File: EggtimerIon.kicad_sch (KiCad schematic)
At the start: 46 parts, among them J1 Conn_01x02, J2 Conn_01x03, J3 B2B-PH-K-S, J4 USB_C_Receptacle_USB2.0, Q1 IRLML6244, Q2 2N7002, Q3 2N7002, U1 ESP32-WROOM-32-N4, U2 MPU-6050, U3 MS5611-01BA, U4 CAT24C512XI-T2, U5 AP2112K-3.3, U6 CP2102N-Axx-xQFN28

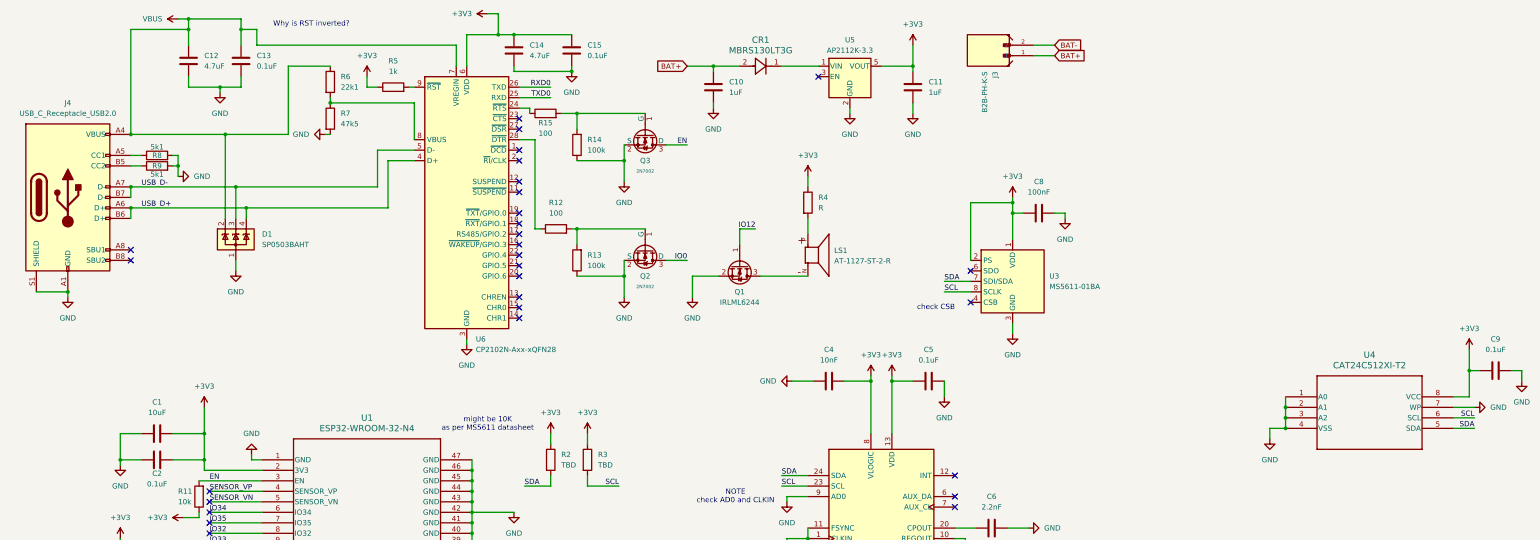
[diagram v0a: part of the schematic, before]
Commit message: Removed Bridge and Flash
Deleted USB C Connector
Deleted EEPROM
Deleted USB to UART Bridge and external circuitry
Added mounting holes
Added changes to layout
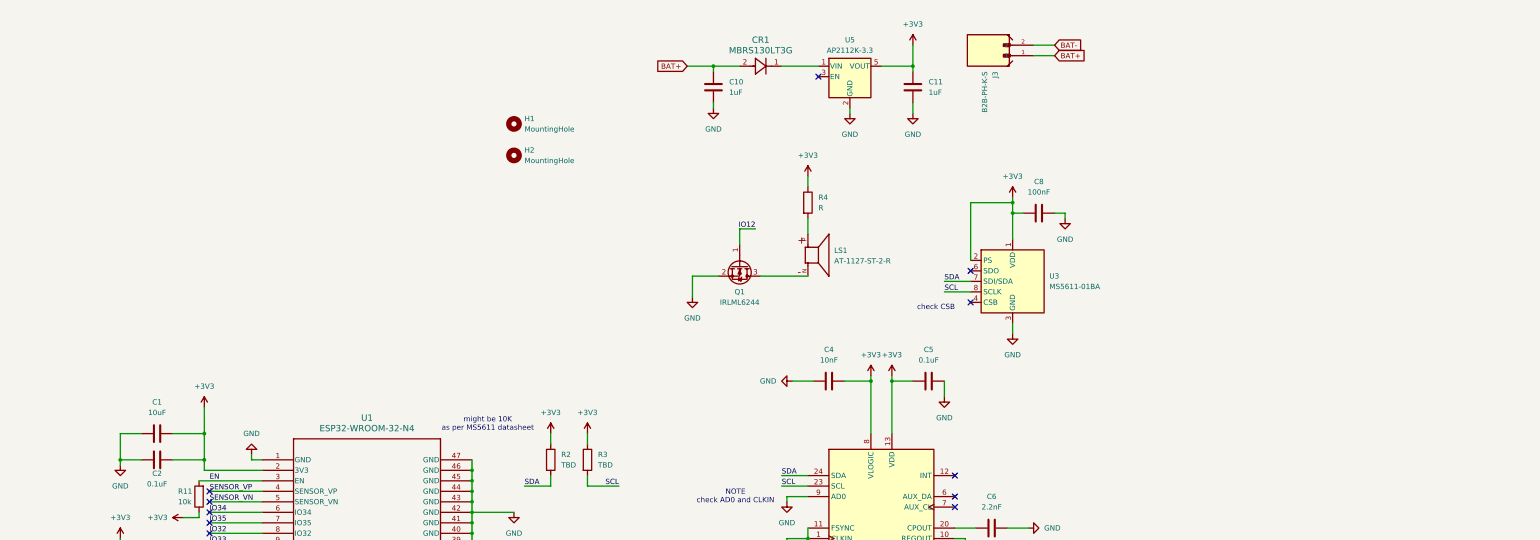
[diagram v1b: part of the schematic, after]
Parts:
- removed C12, C14: 4.7uF, PCM_JLCPCB:C_1206, symbol Device:C
- removed C13, C15, C9: 0.1uF, PCM_JLCPCB:C_1206, symbol Device:C
- removed D1: SP0503BAHT, Package_TO_SOT_SMD:SOT-143, symbol Power_Protection:SP0503BAHT
- removed J4: USB_C_Receptacle_USB2.0, Connector_USB:USB_C_Receptacle_G-Switch_GT-USB-7010ASV, symbol USBCCOnn:USB_C_Receptacle_USB2.0
- removed Q2, Q3: 2N7002, PCM_JLCPCB:Q_SOT-23, symbol PCM_JLCPCB-Transistors:NMOS,2N7002
- removed R12, R15: 100, PCM_JLCPCB:R_1206, symbol Device:R
- removed R13, R14: 100k, PCM_JLCPCB:R_1206, symbol Device:R
- removed R5: 1k, PCM_JLCPCB:R_1206, symbol Device:R
- removed R6: 22k1, PCM_JLCPCB:R_1206, symbol Device:R
- removed R7: 47k5, PCM_JLCPCB:R_1206, symbol Device:R
- removed R8, R9: 5k1, PCM_JLCPCB:R_1206, symbol Device:R
- removed U4: CAT24C512XI-T2, CAT24C512:SOIC8_ONS, symbol CAT24C512:CAT24C512XI-T2
- removed U6: CP2102N-Axx-xQFN28, Package_DFN_QFN:QFN-28-1EP_5x5mm_P0.5mm_EP3.35x3.35mm, symbol Interface_USB:CP2102N-Axx-xQFN28
- added H1, H2: MountingHole, PCM_JLCPCB:Hole, 3mm, symbol Mechanical:MountingHole
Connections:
- no-connect marks 50 -> 32
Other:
- note removed: "Why is RST inverted?"

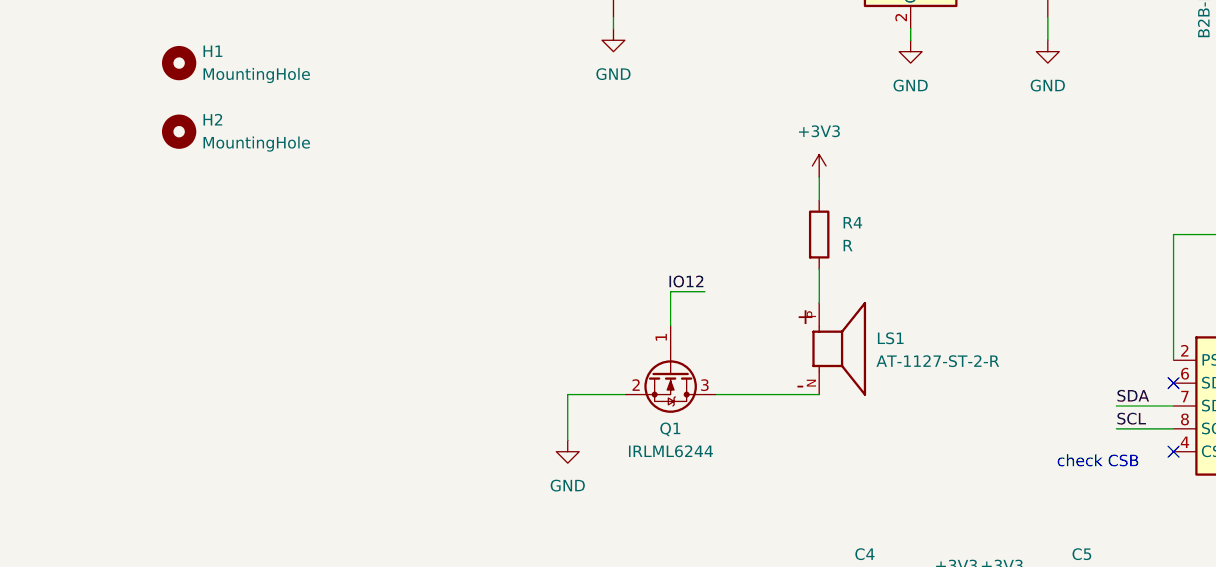
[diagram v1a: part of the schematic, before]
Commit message: Major Updates
- Moved all components to front side
- Added third mounting hole
- Added most JLC #'s to components
- Replaced buzzer with one in stock
- Changed passive components from 1206 to 0402 for assembly
- Replaced components based on schematic
- Added zones for power and ground pours
- Routed tracks and vias
- Removed designator silk and added labels to jumper pins
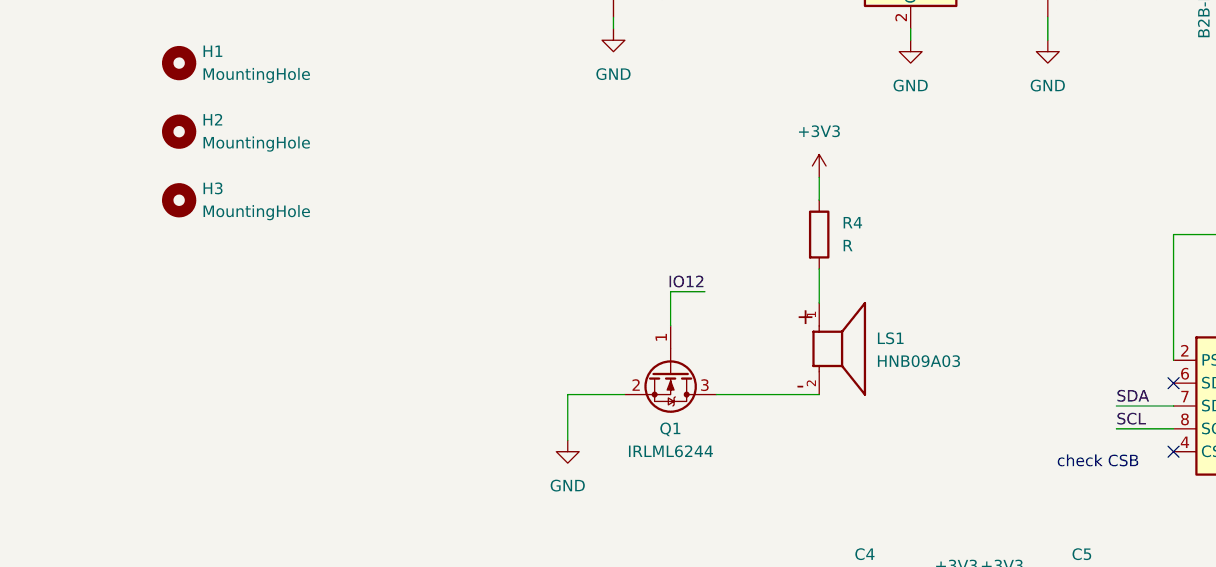
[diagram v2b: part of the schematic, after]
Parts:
- added H3: MountingHole, PCM_JLCPCB:Hole, 3mm, symbol Mechanical:MountingHole
- C1: footprint PCM_JLCPCB:C_1206 -> Capacitor_SMD:C_0402_1005Metric; LCSC (none) -> C15525
- C10, C11: footprint PCM_JLCPCB:C_1206 -> Capacitor_SMD:C_0402_1005Metric; LCSC (none) -> C52923
- C2, C5, C7, C8: footprint PCM_JLCPCB:C_1206 -> Capacitor_SMD:C_0402_1005Metric; LCSC (none) -> C1525
- C3: footprint PCM_JLCPCB:C_1206 -> Capacitor_SMD:C_0402_1005Metric
- C4: footprint PCM_JLCPCB:C_1206 -> Capacitor_SMD:C_0402_1005Metric; LCSC (none) -> C15195
- C6: footprint PCM_JLCPCB:C_1206 -> Capacitor_SMD:C_0402_1005Metric; LCSC (none) -> C12530
- J3: LCSC (none) -> C131337
- LS1: value AT-1127-ST-2-R -> HNB09A03; footprint AT-1127-ST-2-R:XDCR_AT-1127-ST-2-R -> HNB09A03:HNB09A03; LCSC (none) -> C96102
- Q1: LCSC (none) -> C5123965
- R1, R2, R3, R4: footprint PCM_JLCPCB:R_1206 -> Capacitor_SMD:C_0402_1005Metric
- R10, R11: footprint PCM_JLCPCB:R_1206 -> Capacitor_SMD:C_0402_1005Metric; LCSC (none) -> C25744
- U2: LCSC (none) -> C24112
- U5: LCSC (none) -> C3021085
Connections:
- net at R4.2: now also LS1.1; no longer LS1.P
- net at Q1.3 (D): now also LS1.2; no longer LS1.N

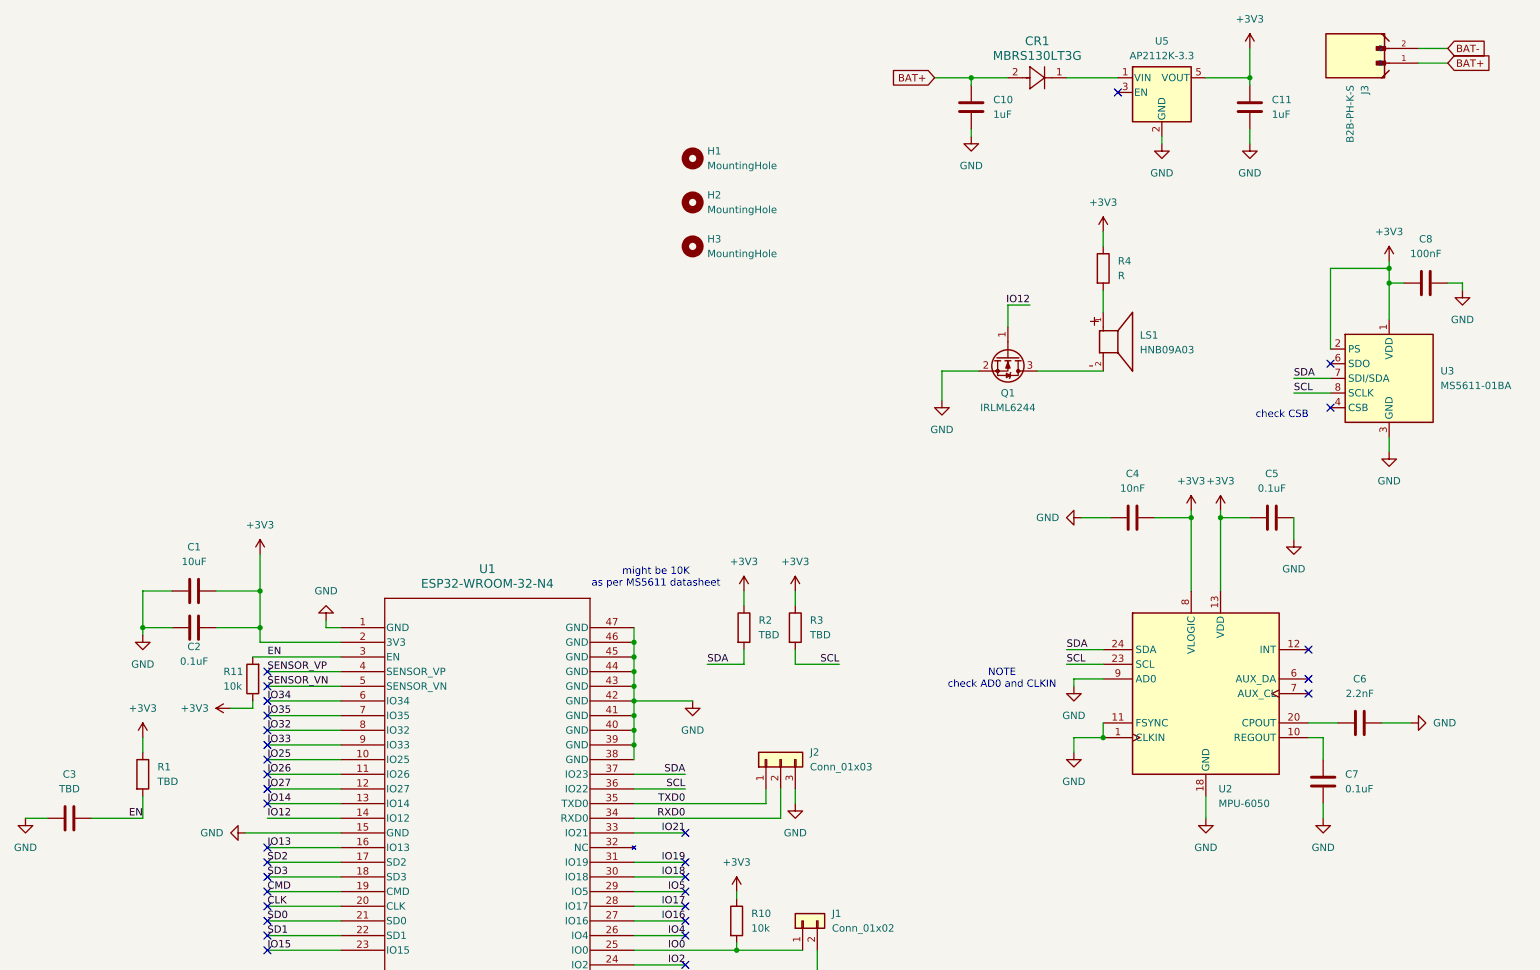
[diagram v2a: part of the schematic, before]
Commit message: Refined Schematic
- determined TBD values
- connected MS5611 CSB pin to GND
- added LEDs to GPIO and power
- added LCSC numbers for new parts
- assigned footprints for new parts
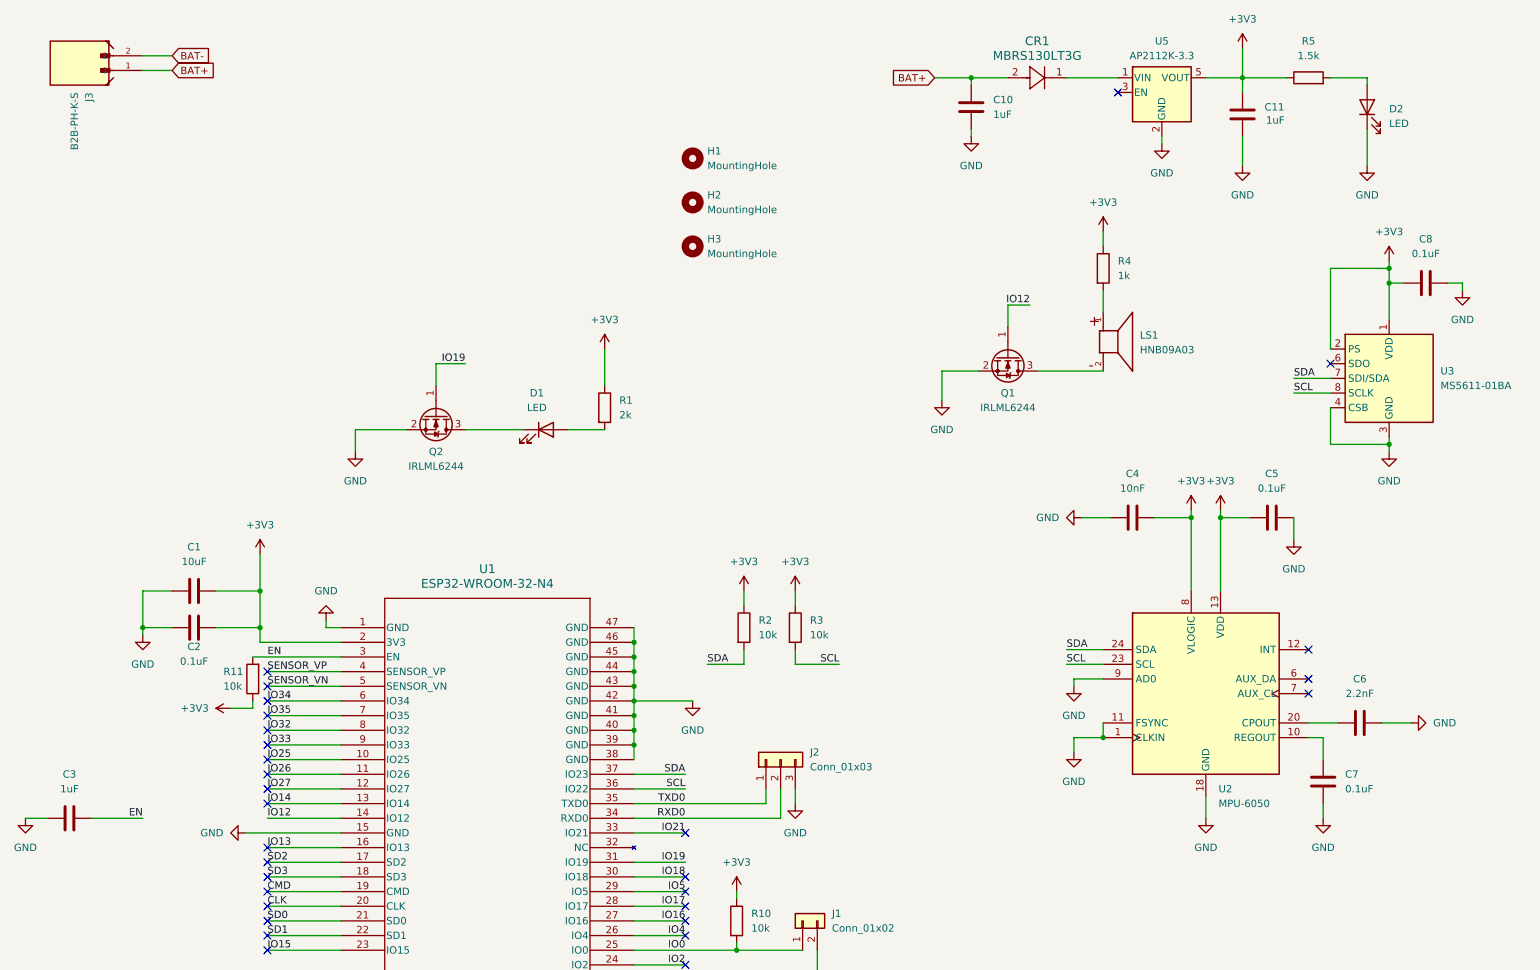
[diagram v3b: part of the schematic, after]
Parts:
- added D1, D2: LED, LED_SMD:LED_0603_1608Metric, symbol Device:LED
- added Q2: IRLML6244, Package_TO_SOT_SMD:SOT-23, symbol Transistor_FET:IRLML6244
- added R5: 1.5k, Capacitor_SMD:C_0402_1005Metric, symbol Device:R
- C3: value TBD -> 1uF
- C8: value 100nF -> 0.1uF
- R1: value TBD -> 2k; LCSC (none) -> C4109
- R2, R3: value TBD -> 10k; LCSC (none) -> C25744
- R4: value R -> 1k; LCSC (none) -> C11702
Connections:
- net +3V3: now also R5.1
- net EN: no longer R1.2
- net GND: now also U3.4 (CSB), U3.5 (CSB), D2.1 (K), Q2.2 (S)
- net IO19: now also Q2.1 (G)
- new net: D1.1 (K), Q2.3 (D)
- new net: D2.2 (A), R5.2
- new net: D1.2 (A), R1.2
- no-connect marks 32 -> 30
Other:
- note removed: "NOTE check AD0 and CLKIN"
- note removed: "check CSB"
- note removed: "might be 10K as per MS5611 datasheet"
- moved on the sheet: C11, J3

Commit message: work
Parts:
- removed C3: 1uF, Capacitor_SMD:C_0402_1005Metric, symbol Device:C
- removed D2: LED, LED_SMD:LED_0603_1608Metric, symbol Device:LED
- removed J1: Conn_01x02, Connector_PinHeader_2.54mm:PinHeader_1x02_P2.54mm_Vertical, symbol Connector_Generic:Conn_01x02
- removed J2: Conn_01x03, Connector_PinHeader_2.54mm:PinHeader_1x03_P2.54mm_Vertical, symbol Connector_Generic:Conn_01x03
- removed R10: 10k, Capacitor_SMD:C_0402_1005Metric, symbol Device:R
- removed U1: ESP32-WROOM-32-N4, RF_Module:ESP32-WROOM-32, symbol ESP32-WROOM-32-N4:ESP32-WROOM-32-N4
- added C9: 1u, Capacitor_SMD:C_0603_1608Metric, symbol Morten_Library.kicad_sym_9:C_Small
- added D5: GREEN, LED_SMD:LED_0603_1608Metric, symbol Morten_Library.kicad_sym_9:LED_Small
- added J4: USB_C_Receptacle_USB2.0_16P, Connector_USB:USB_C_Receptacle_Palconn_UTC16-G, symbol Connector:USB_C_Receptacle_USB2.0_16P
- added R12, R6: 5.1k, Resistor_SMD:R_0402_1005Metric, symbol Device:R
- added R16, R17: 27, Resistor_SMD:R_0402_1005Metric, symbol Device:R
- added R8: 1K, Resistor_SMD:R_0402_1005Metric, symbol Morten_Library.kicad_sym_9:R_Small
- added SW1: RESET, Button_Switch_SMD:SW_SPST_B3U-1000P, symbol Morten_Library.kicad_sym_9:SW_SPST
- added SW2: BOOT, Button_Switch_SMD:SW_SPST_B3U-1000P, symbol Morten_Library.kicad_sym_9:SW_SPST
- added U4: ESP32-S3-WROOM-1-N8, RF_Module:ESP32-S3-WROOM-1, symbol Morten_Library.kicad_sym_9:ESP32-S3-WROOM-1x-N8R8
- R5: value 1.5k -> 10k; LCSC C25867 -> C25744
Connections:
- net EN is gone; now on net +3V3: R11.2
- net +3V3: now also R5.2, R8.1, U4.2 (3V3); no longer R11.1, R5.1
- net GND: now also C9.2, D5.1 (K), J4.A1 (GND), J4.A12 (GND), J4.B1 (GND), J4.B12 (GND), J4.S1 (SHIELD), R12.2, R6.1, SW1.1 (A), SW2.1 (A), U4.1 (GND), U4.40 (GND), U4.41 (EPAD(GND))
- net SCL: now also U4.17 (GPIO9)
- net SDA: now also U4.12 (GPIO8)
- net IO12 renamed BUZZER
- net BUZZER: now also U4.33 (GPIO40)
- net IO19 renamed LED
- net LED: now also U4.32 (GPIO39)
- new net: J4.A4 (VBUS), J4.A9 (VBUS), J4.B4 (VBUS), J4.B9 (VBUS)
- new net: J4.A5 (CC1), R6.2
- new net: J4.B5 (CC2), R12.1
- new net: D5.2 (A), R8.2
- new net: R5.1, U4.15 (GPIO3)
- new net ESP_EN: C9.1, R11.1, SW1.2 (B), U4.3 (EN)
- new net ESP_IO0: SW2.2 (B), U4.27 (GPIO0)
- new net USB_D+: J4.A6 (D+), J4.B6 (D+), R16.1, R16.2, U4.14 (GPIO20/USB_D+)
- new net USB_D-: J4.A7 (D-), J4.B7 (D-), R17.1, R17.2, U4.13 (GPIO19/USB_D-)
- no-connect marks 30 -> 36
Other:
- note added: "BOOT SWITCH"
- note added: "LDO"
- note added: "MCU USB"
- moved on the sheet: C1, C10, C11, C2, C4, C5, C6, C7, C8, CR1, D1, H1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

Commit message: Updates
work towards S3 module
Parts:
- removed D5: GREEN, LED_SMD:LED_0603_1608Metric, symbol Morten_Library.kicad_sym_9:LED_Small
- removed R8: 1K, Resistor_SMD:R_0402_1005Metric, symbol Morten_Library.kicad_sym_9:R_Small
- added D2: LED, LED_SMD:LED_0603_1608Metric, symbol Device:LED
- added R7: 1.5k, Capacitor_SMD:C_0402_1005Metric, symbol Device:R
- CR1: footprint MBRS130L3TG:DIODE_SMB_2L_ONS -> Diode:DIODE_SMB_2L_ONS
- U5: footprint Package_TO_SOT_SMD:SOT-23-5 -> LDO:SOT_RG1_DIO
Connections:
- net +3V3: now also R7.1
- net GND: now also D2.1 (K)
- new net: D2.2 (A), R7.2

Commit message: Routing Updates to parts
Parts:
- removed C9: 1u, Capacitor_SMD:C_0603_1608Metric, symbol Morten_Library.kicad_sym_9:C_Small
- removed Q2: IRLML6244, Package_TO_SOT_SMD:SOT-23, symbol Transistor_FET:IRLML6244
- added C3: 1uF, Capacitor_SMD:C_0402_1005Metric, symbol Device:C
- H1, H2, H3: now not fitted
- J4: LCSC (none) -> C2765186
- R12, R6: LCSC (none) -> C25905
- R16, R17: LCSC (none) -> C25100
- R2, R3: value 10k -> 4.7k; LCSC C25744 -> C25900
- SW1, SW2: LCSC (none) -> C231329
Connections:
- net +3V3: no longer R1.1
- net ESP_EN: now also C3.1
- net GND: now also D1.1 (K), C3.2
- net LED: now also R1.1

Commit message: updates
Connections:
- net BAT- is gone; now on net GND: J3.2
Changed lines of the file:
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@@
+	(wire
+		(pts
+			(xy 207.01 36.83) (xy 214.63 36.83)
+		)
+		(stroke
+			(width 0)
+			(type default)
+		)
+	)
 	(wire
 		(pts
@@
 	(label "USB_D-"
 		(at 260.35 100.33 180)
+		(effects
+			(font
+				(size 1.27 1.27)
+			)
+			(justify right bottom)
+		)
+	)
+	(label "GND"
+		(at 214.63 36.83 180)
 		(effects
 			(font
@@
 			(effects
 				(font
+					(size 1.27 1.27)
+				)
+				(justify right)
+				(hide yes)
+			)
+		)
+	)
+	(global_label "BAT-"
+		(shape input)
+		(at 207.01 36.83 180)
+		(fields_autoplaced yes)
+		(effects
+			(font
+				(size 1.27 1.27)
+			)
+			(justify right)
+		)
+		(property "Intersheetrefs" "${INTERSHEET_REFS}"
+			(at 199.1262 36.83 0)
+			(effects
+				(font

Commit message: Update Footprints
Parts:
- C6: LCSC C12530 -> C84703
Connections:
- net +3V3: now also U5.3 (EN)
- no-connect marks 36 -> 35
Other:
- moved on the sheet: C4, C5, C6, C7, U2
